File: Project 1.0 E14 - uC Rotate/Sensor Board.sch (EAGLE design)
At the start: 94 parts, among them IC1 LT1963EST-1.5, IC2 LT1963EST-1.5, IC4 LT1963EST-1.5

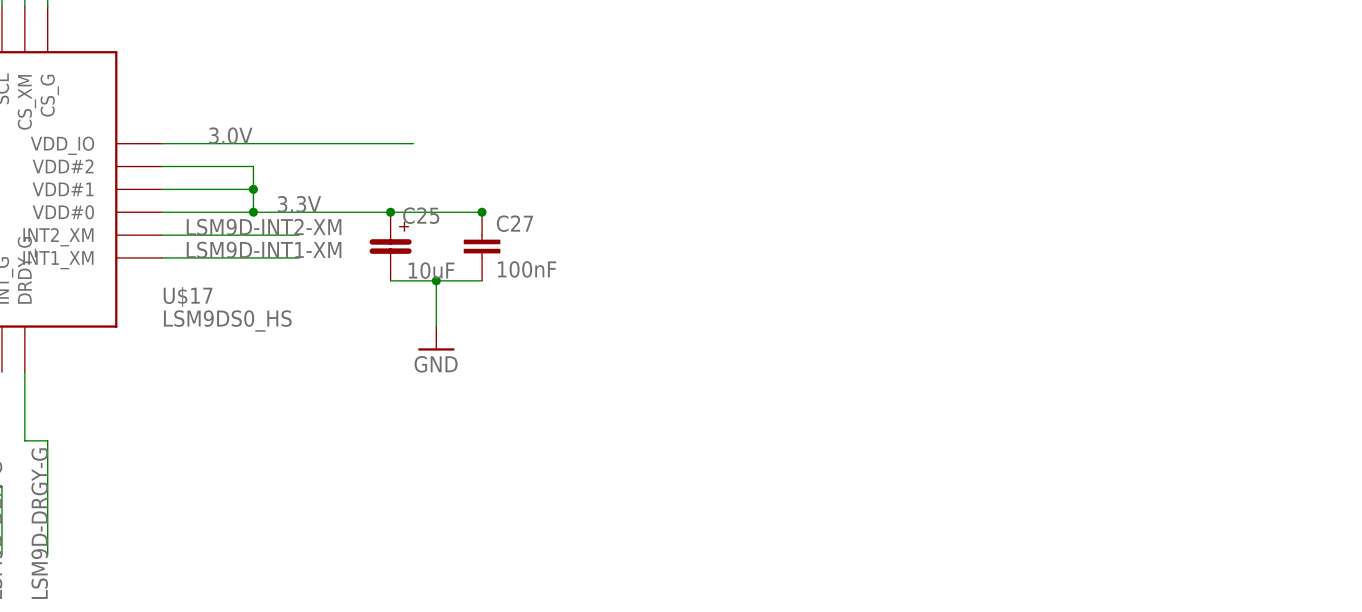
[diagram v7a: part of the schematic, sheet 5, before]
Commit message: Sensor Test Board: Added humidity sensor to the I2C lines. Changed packages from hand solder to oven, and corrected small missalignment in some packages. Two humidity sensors and one crystal were added to the libraries
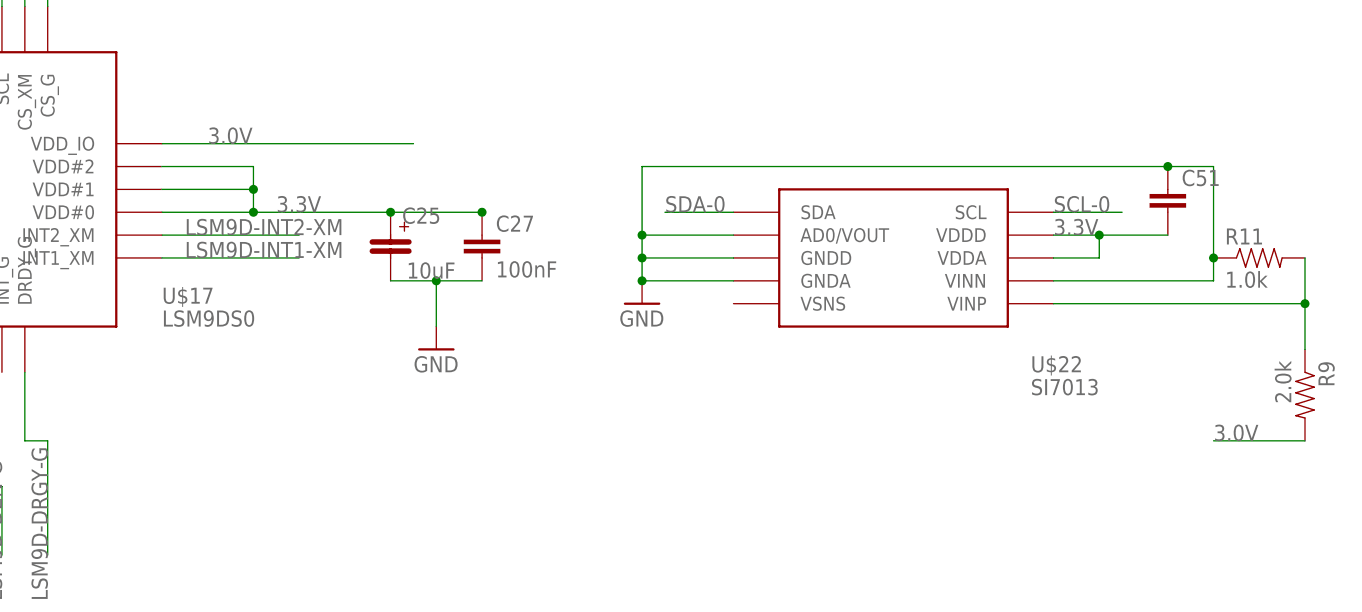
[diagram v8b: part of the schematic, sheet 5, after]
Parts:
- added C51: (no value), Kas-Passives:CAPACITOR0402
- added R11: 1.0k, Kas-Passives:RESISTOR
- added R9: 2.0k, Kas-Passives:RESISTOR
- added U$22: SI7013, Kas-Sensors:SI7013
- C1, C10, C11, C12, C14, C15, C16, C17, C18, C2, C20, C21, C23, C24, C26, C27, C28, C29, C3, C30, C31, C32, C33, C34, C35, C36, C37, C38, C39, C4, C40, C41, C42, C43, C44, C48, C49, C5, C52, C6, C8, C9: device Kas-Passives:CAPACITOR -> Kas-Passives:CAPACITOR0402
- U$1: value MAG3110_HS -> MAG3110; device Kas-Sensors:MAG3110_HS -> Kas-Sensors:MAG3110
- U$10: device Kas-Sensors:ADXL362_HS -> Kas-Sensors:ADXL362
- U$13: device Kas-Crystal:NX5032GA -> Kas-Crystal:NX3225GA
- U$17: value LSM9DS0_HS -> LSM9DS0; device Kas-Sensors:LSM9DS0_HS -> Kas-Sensors:LSM9DS0
- U$19: value MAX21000_HS -> MAX21000; device Kas-Sensors:MAX21000_HS -> Kas-Sensors:MAX21000
- U$2: value H3LIS331DLTR_HS -> H3LIS331DLTR; device Kas-Sensors:H3LIS331DLTR_HS -> Kas-Sensors:H3LIS331DLTR
- U$3: value L3GD20H_HS -> L3GD20H; device Kas-Sensors:L3GD20H_HS -> Kas-Sensors:L3GD20H
- U$4: value LPS331AP_HS -> LPS331AP; device Kas-Sensors:LPS331AP_HS -> Kas-Sensors:LPS331AP
- U$5: value MPL3115A2_HS -> MPL3115A2; device Kas-Sensors:MPL3115A2_HS -> Kas-Sensors:MPL3115A2
- U$6: value LSM303D_HS -> LSM303D; device Kas-Sensors:LSM303D_HS -> Kas-Sensors:LSM303D
- U$9: device Kas-Sensors:LIS3DH_HS -> Kas-Sensors:LIS3DH
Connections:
- new net N$18: R11.2, R9.1, U$22.VINP
- net 3.0V: now also R9.2
- net 3.3V: now also C51.2, U$22.VDDA, U$22.VDDD
- net GND: now also C51.1, R11.1, U$22.AD0/VOUT, U$22.GNDA, U$22.GNDD, U$22.VINN
- net N$14: now also U$13.A; no longer U$13.P$1
- net N$16: now also U$13.B; no longer U$13.P$2
- net SCL-0: now also U$22.SCL
- net SDA-0: now also U$22.SDA
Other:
- moved on the sheet: C43, C44
